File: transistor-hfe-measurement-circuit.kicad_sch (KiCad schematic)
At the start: 97 parts, among them J1 Barrel_Jack_Switch, J2 B-057-HP, J3 B-057-HP, J4 2227MC-06-03, J5 B-057-HP, J6 B-057-HP, Q1 HL2303, Q2 SS8550 Y2, Q3 HL2303, Q4 SSM6L56FE, SW1 SW_DPDT_x2, SW2 SW_DPDT_x2, U1 NJM11100F1, U2 74HC14D,653, U3 OPA2333AIDR, U4 REF35102QDBVR

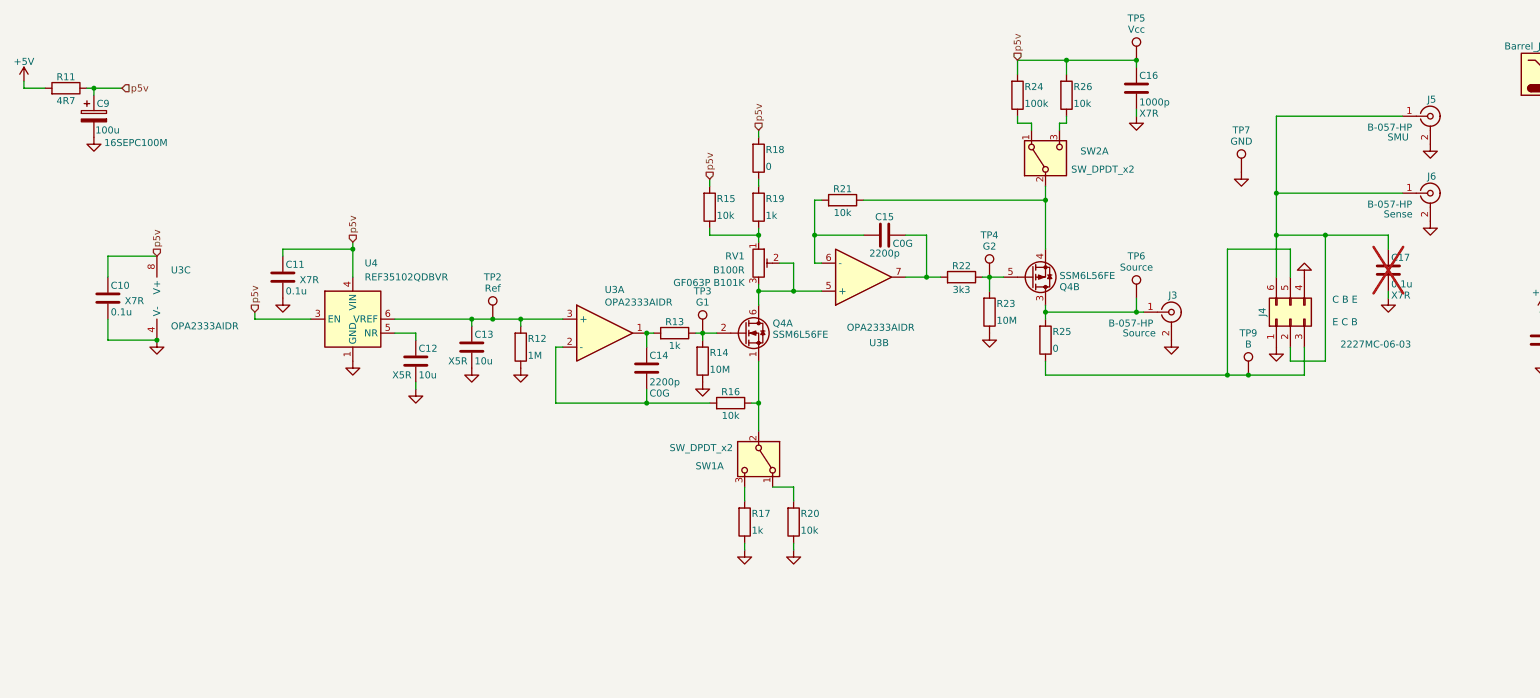
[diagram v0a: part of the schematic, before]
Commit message: feat: v1.1 として現行版の定電流回路を取り込む
HVRF リポジトリの作業ツリー（2026-10-15 時点）を v1.1 として取り込む。

- プロジェクトを transistor-hfe-measurement-circuit に改名
  （サブシートは cc-component.kicad_sch）
- 回路図・PCB のタイトルブロックに版数・著作権・ライセンス
  （CERN-OHL-P v2）・リポジトリ URL を入れる
- 基板シルクの版数を V1.0 から V1.1 にする
- PCB にはメーカー製 3D モデルを埋め込まず、DC ジャックは自作の
  簡易モデルを参照する

Co-Authored-By: Claude Opus 5.5 <noreply@anthropic.com>
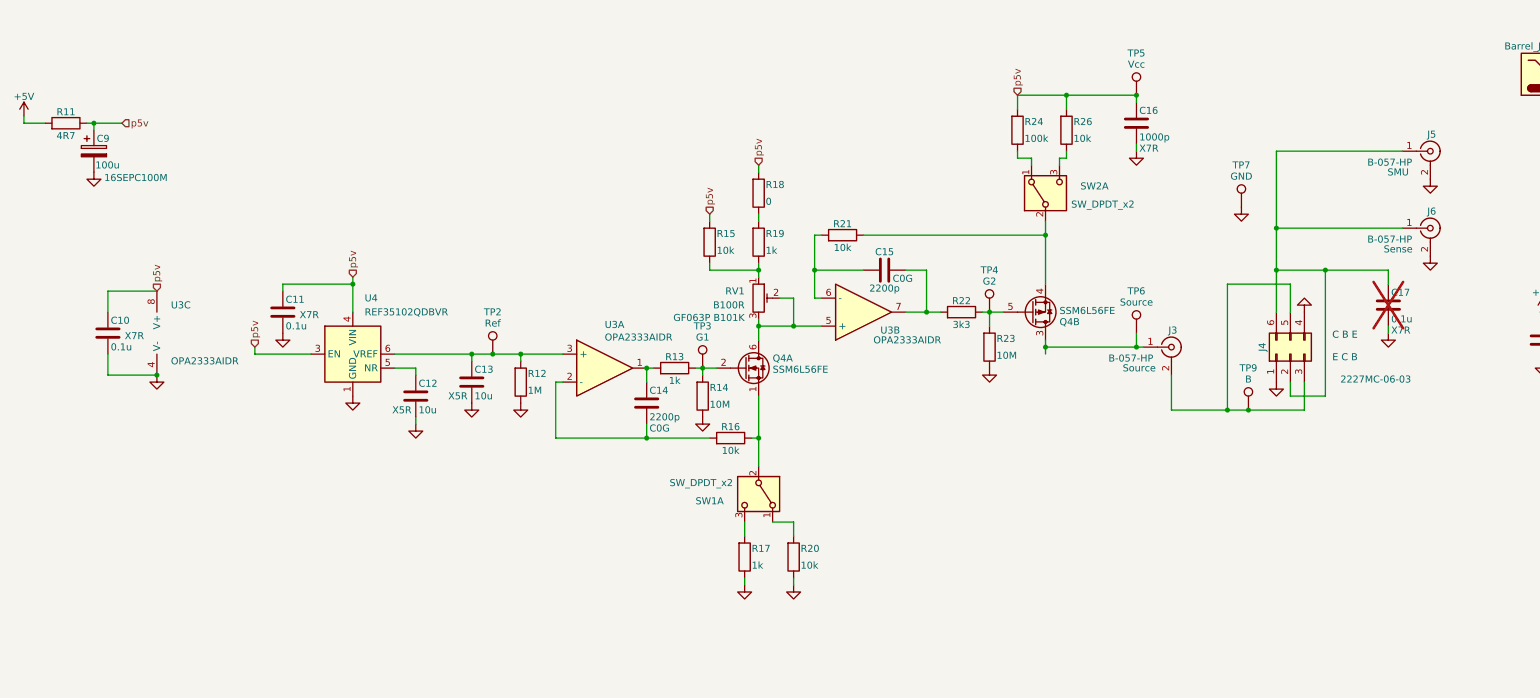
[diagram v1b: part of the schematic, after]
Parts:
- removed R25: 0, Resistor_SMD:R_0603_1608Metric, symbol 3_JLCPCB_BasicParts:R_0603_0_Vertical
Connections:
- net GNDPWR: no longer J3.2 (Ext)
- net at J4.3 (Pin_3), J4.5 (Pin_5), TP9.1: now also J3.2 (Ext)
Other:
- company: (none) -> Hayata Yamamoto
- title: Anthracite (Top) -> Transistor hFE Measurement Circuit Schematic
- moved on the sheet: C10, C11, C12, C13, C14, C15, C16, C17, C9, J3, J4, J5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
